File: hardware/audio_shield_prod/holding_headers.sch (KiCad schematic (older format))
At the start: 34 parts, among them J10 Conn_01x02_Male, J11 Conn_01x02_Male, J12 Conn_01x02_Male, J13 Conn_01x02_Male, J14 Conn_01x02_Male, J15 Conn_01x02_Male, J16 Conn_01x02_Male, J17 Conn_01x02_Male, J18 Conn_01x02_Male, J19 Conn_01x02_Male, J20 Conn_01x02_Male, J21 Conn_01x02_Male, J22 Conn_01x02_Male, J23 Conn_01x02_Male, J24 Conn_01x02_Male, J25 Conn_01x02_Male, J26 Conn_01x02_Male, J27 Conn_01x02_Male, J28 Conn_01x02_Male, J29 Conn_01x02_Male, J30 Conn_01x02_Male, J31 Conn_01x02_Male, J32 Conn_01x02_Male, J33 Conn_01x02_Male, J34 Conn_01x02_Male, J35 Conn_01x02_Male, J36 Conn_01x02_Male, J37 Conn_01x02_Male, J38 Conn_01x02_Male, J39 Conn_01x02_Male, J40 Conn_01x02_Male, J41 Conn_01x02_Male, J42 Conn_01x02_Male, J43 Conn_01x02_Male

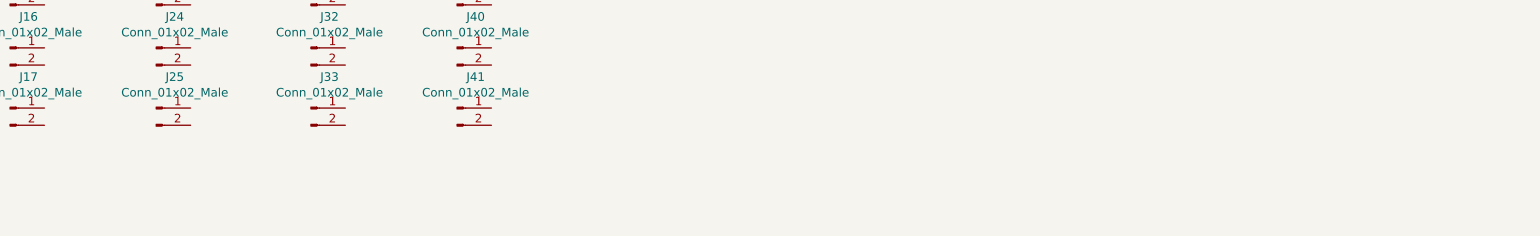
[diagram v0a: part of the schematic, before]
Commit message: Update PCB info after footprint missmatch
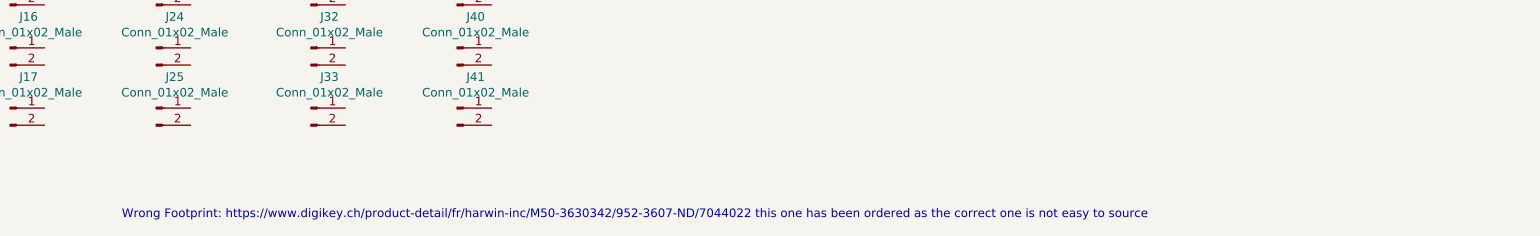
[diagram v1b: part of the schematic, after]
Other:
- note added: "Wrong Footprint: https://www.digikey.ch/product-detail/fr/harwin-inc/M50-3630342/952-3607-ND/7044022 this one has been ordered as the correct one is not easy to source"
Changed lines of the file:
@@
 	1    0    0    -1
 $EndComp
+Text Notes 2150 4850 0    50   ~ 0
+Wrong Footprint: https://www.digikey.ch/product-detail/fr/harwin-inc/M50-3630342/952-3607-ND/7044022 this one has been ordered as the correct one is not easy to source
 $EndSCHEMATC
